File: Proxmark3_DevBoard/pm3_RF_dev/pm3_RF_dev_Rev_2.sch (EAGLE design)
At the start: 96 parts, among them IC10 74XX244-OCTAL-TRISTATE-BUFFERS, IC11 CD4066, IC202 ADC08060, IC3 PQ1X331M2ZP-3V3-LDO-SOT-23-5, IC4 HCU-INVERTER, IC6 MCP6294, IC9 74XX244-OCTAL-TRISTATE-BUFFERS, U201 FB

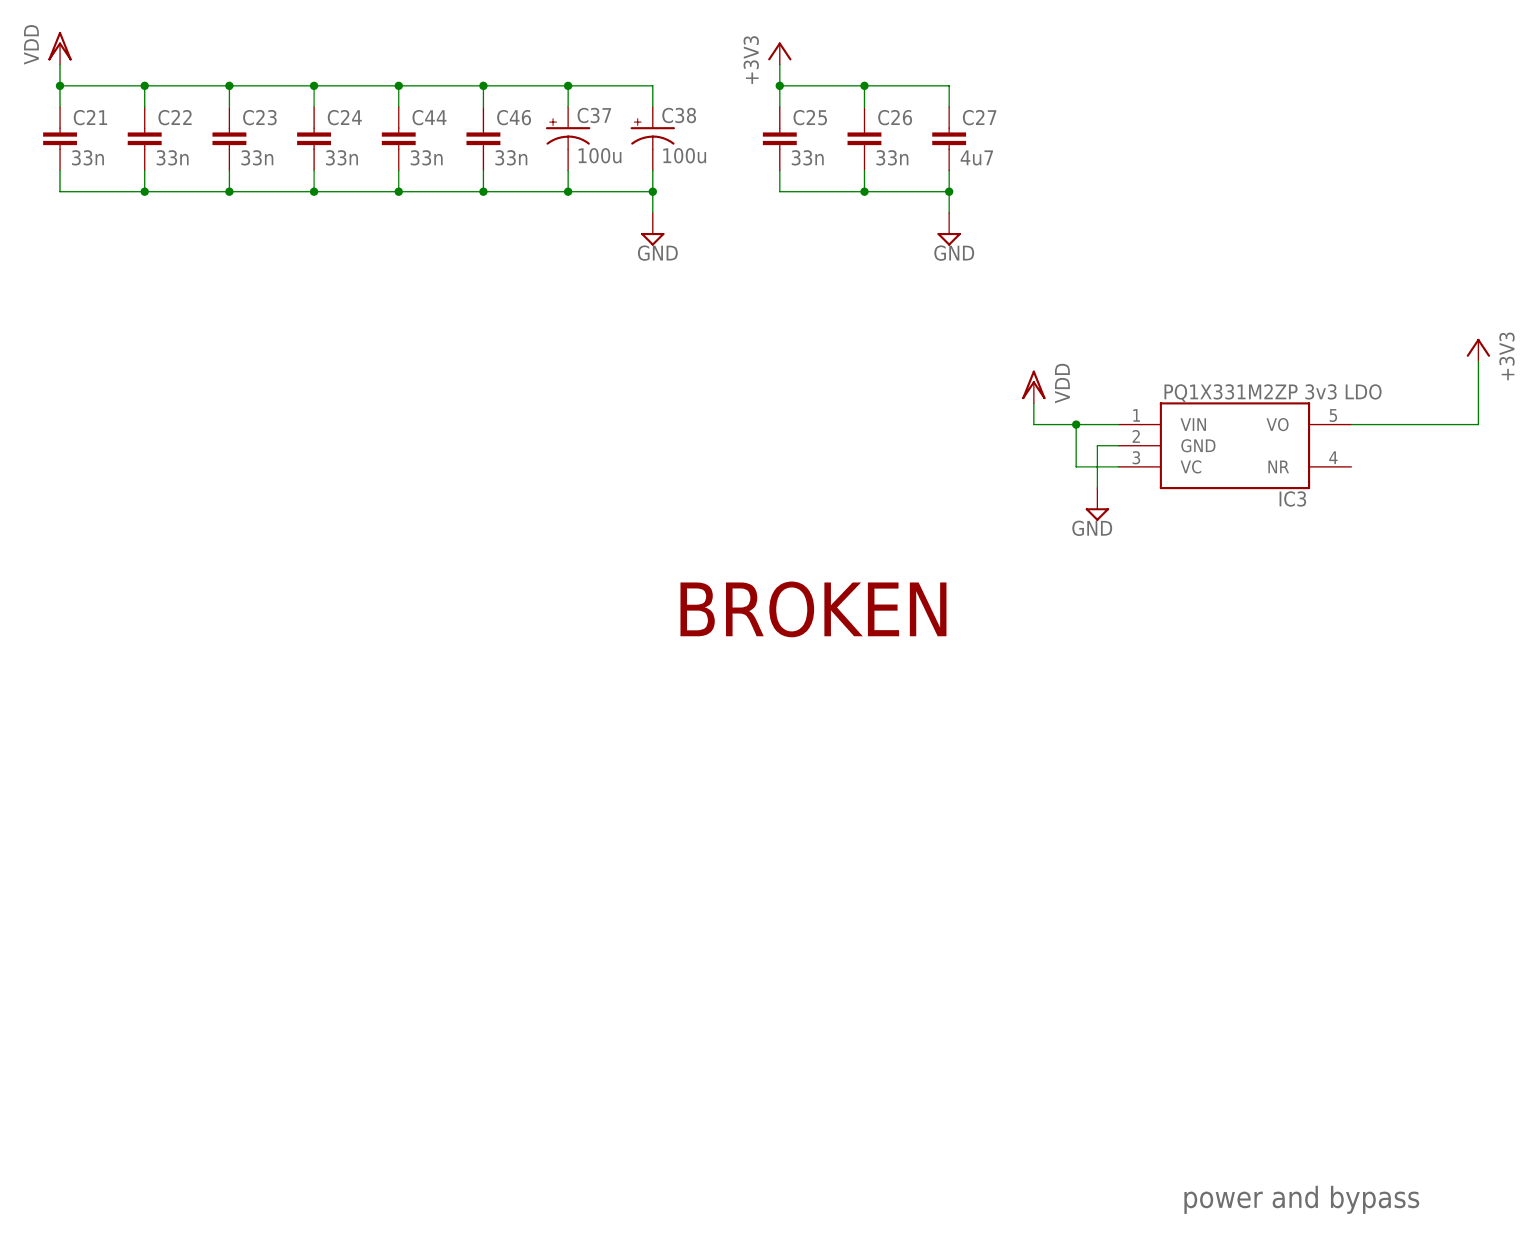
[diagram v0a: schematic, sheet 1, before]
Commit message: 
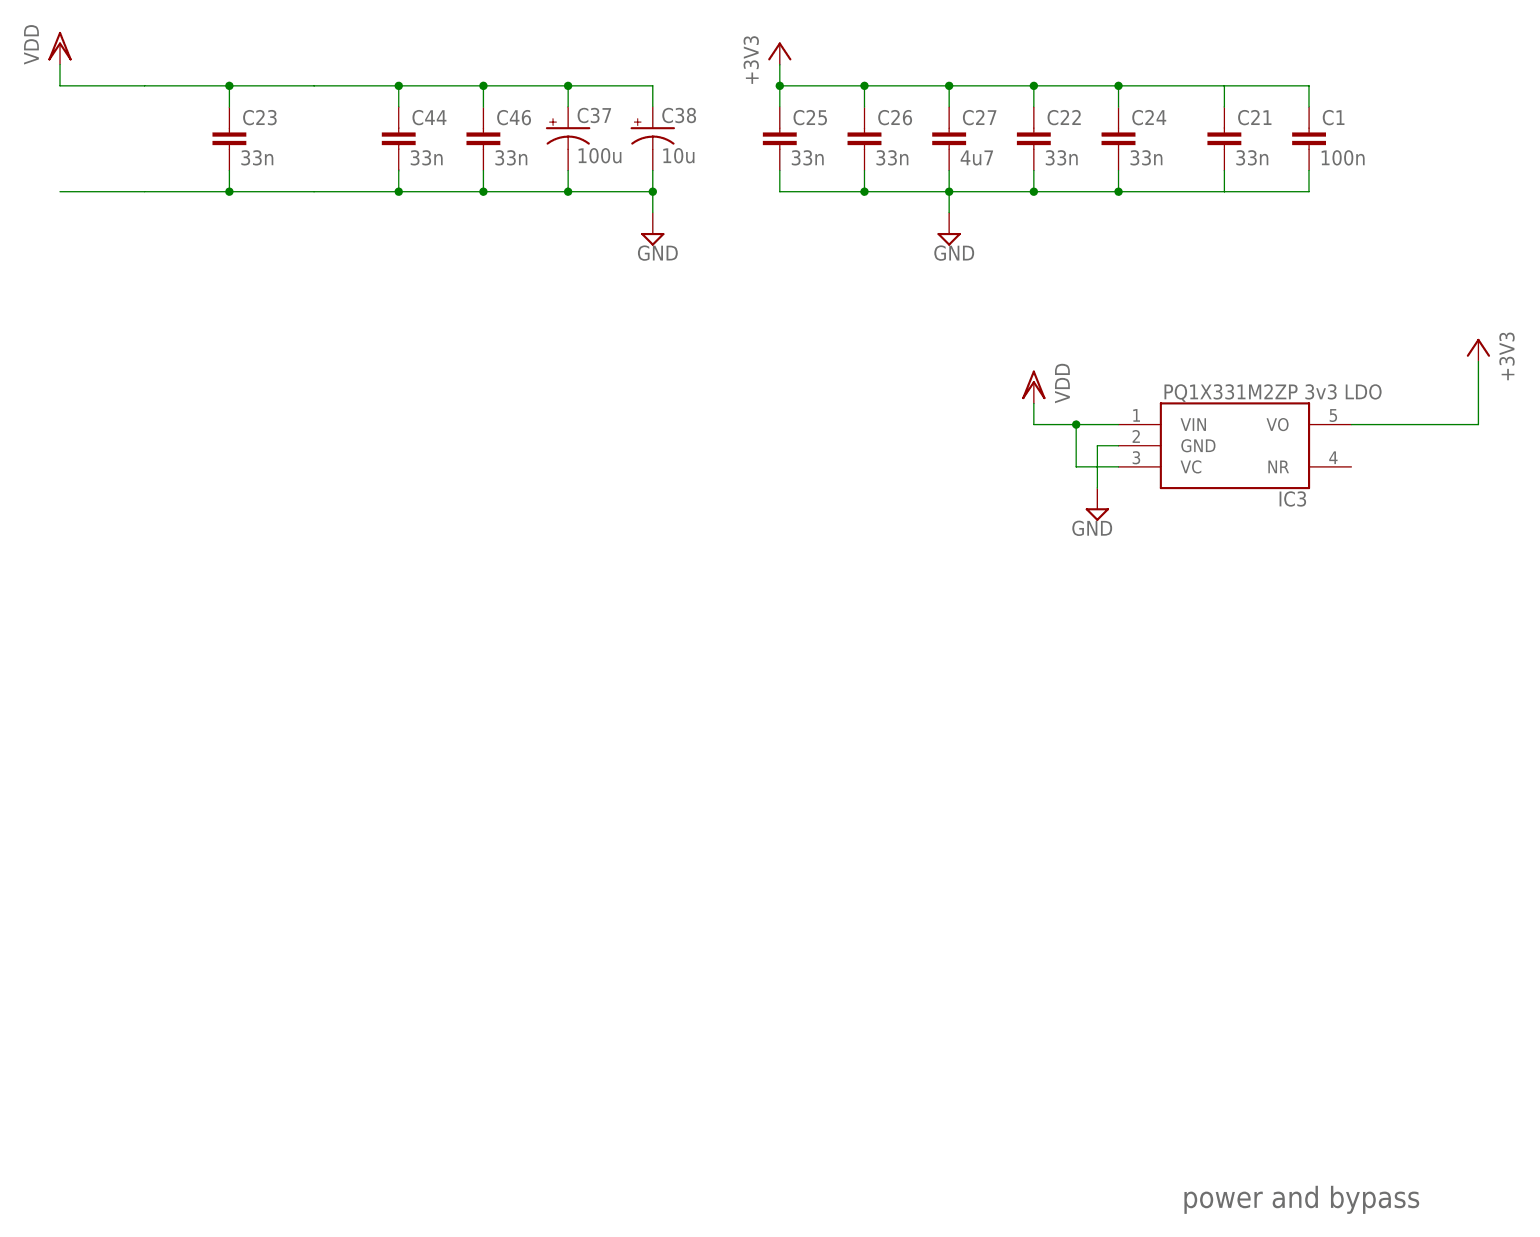
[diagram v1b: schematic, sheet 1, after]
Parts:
- removed C17: dnp, merged:CAPACITOR0603
- added C1: 100n, merged:CAPACITOR0603
- C38: value 100u -> 10u
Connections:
- removed net N$24: C201.2, C207.2, IC202.AGND1, IC202.AGND2, IC202.AGND3, IC202.AGND4, IC202.DGND, IC202.PD, IC202.VINGND, R202.1
- new net VADC: C205.1, C213.1, IC202.VDD, U201.A
- net +3V3: now also C1.1, C21.1, C22.1, C24.1, IC11.VDD, IC6P.V+, R9.2
- net ADCDR_HI: no longer C17.2
- net GND: now also C1.2, C201.2, C207.2, IC202.AGND1, IC202.AGND2, IC202.AGND3, IC202.AGND4, IC202.DGND, IC202.PD, IC202.VINGND, R202.1
- net N$15: no longer C17.1
- net VDD: no longer C205.1, C21.1, C213.1, C22.1, C24.1, IC11.VDD, IC202.VDD, IC6P.V+, R9.2, U201.A
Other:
- note removed: "BROKEN"
- moved on the sheet: C21, C22, C24
